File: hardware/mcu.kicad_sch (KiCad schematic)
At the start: 0 parts

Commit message: MBR0.0.1 - Begin addition of sheet pins to MCU page
Incomplete
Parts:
- added U1: STM32H503RBTx, Package_QFP:LQFP-64_10x10mm_P0.5mm, symbol MCU_ST_STM32H5:STM32H503RBTx
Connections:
- new net: U1.18 (VSS), U1.31 (VSS), U1.47 (VSS), U1.63 (VSS)
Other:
- note added: "Indicates if any thermal switches are open"
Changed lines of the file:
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@@
 	(generator "eeschema")
 	(generator_version "10.0")
-	(paper "A4")
+	(paper "B")
 	(title_block
 		(title "[BOARD NAME]")
@@
 		(company "Formula Slug")
 	)
-)

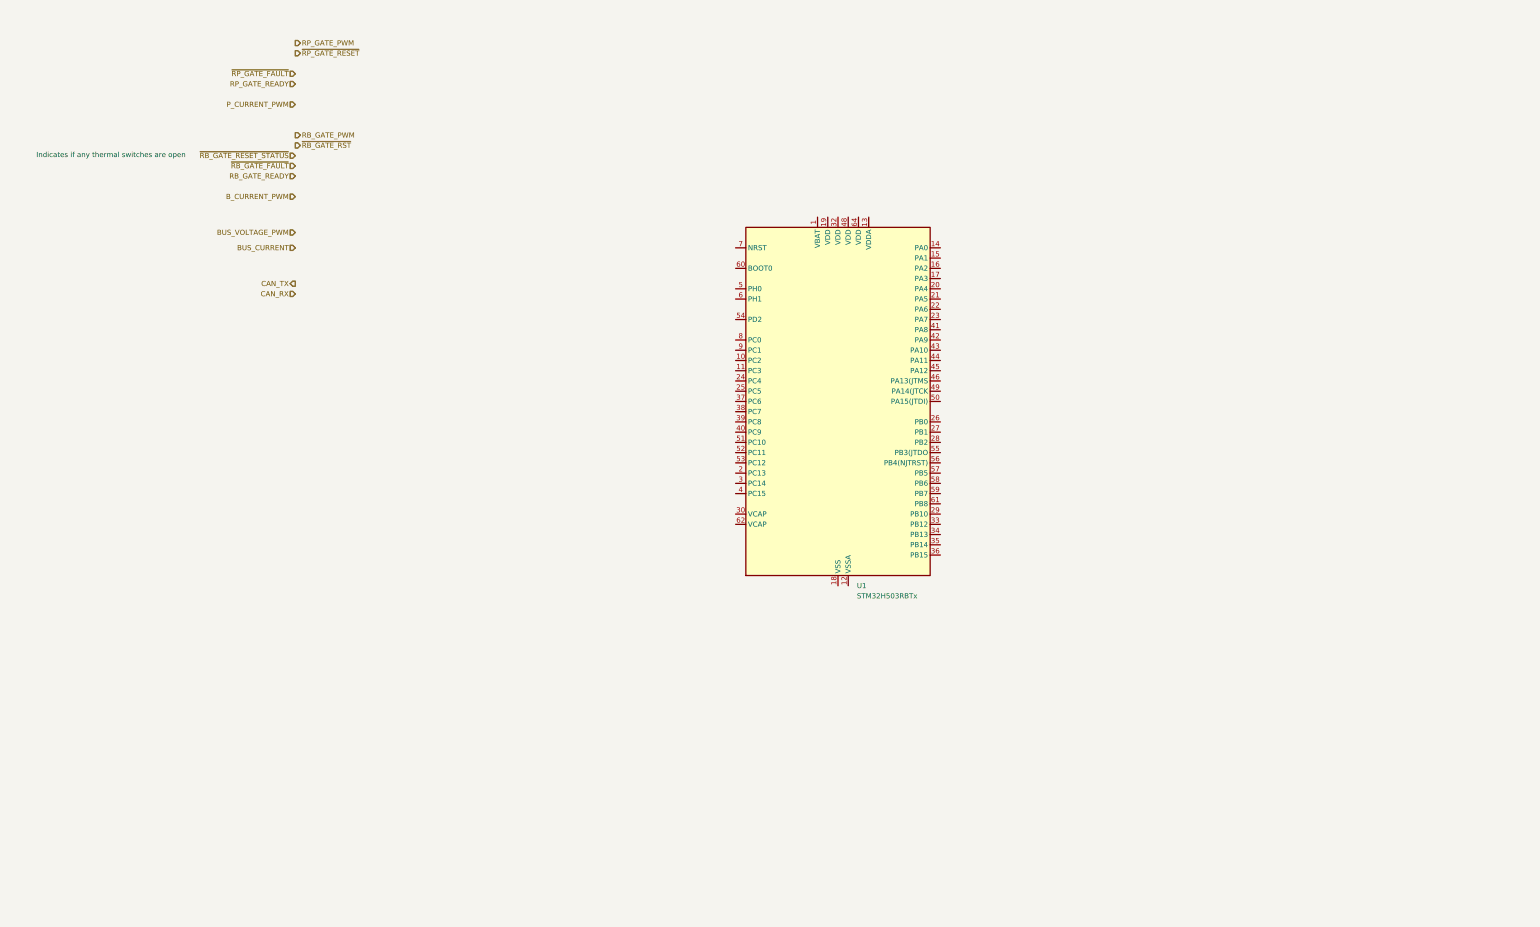
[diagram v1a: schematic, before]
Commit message: R0.0.2 Add more connections to MCU, some connectors
commit d1f92fde9a9b01f608e388bb27e003f4547c4ba5
Author: fezboy <31973884+fezboy@users.noreply.github.com>
Date:   Tue Apr 28 12:29:51 2026 -0700

    R0.0.2 Add more connections to MCU, some connectors
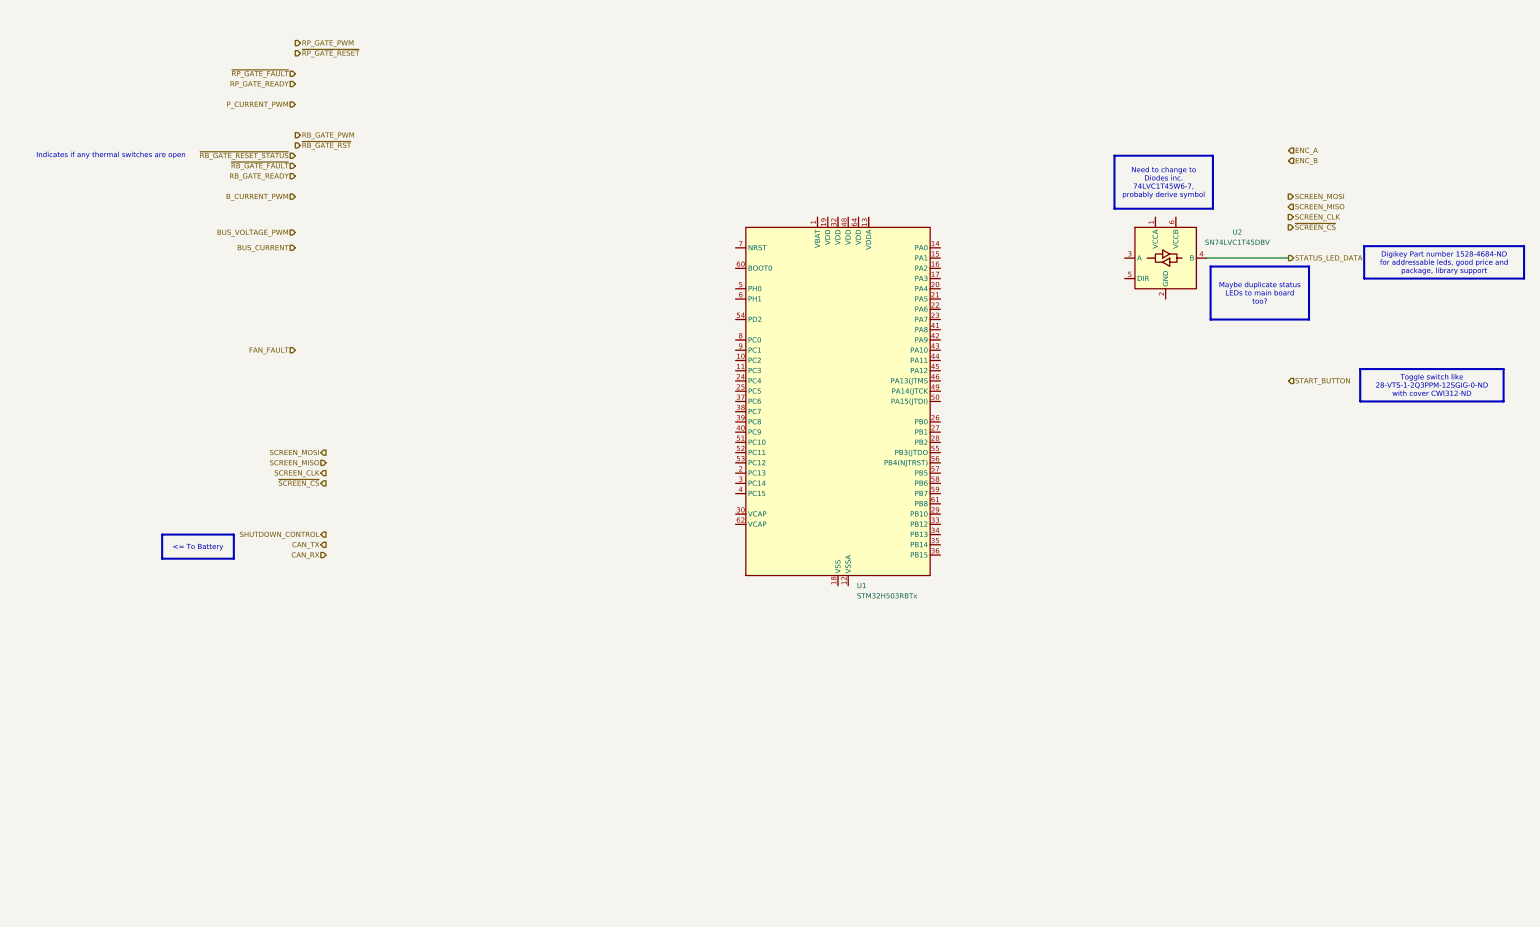
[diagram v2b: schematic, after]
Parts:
- added U2: SN74LVC1T45DBV, Package_TO_SOT_SMD:SOT-23-6, symbol Logic_LevelTranslator:SN74LVC1T45DBV
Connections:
- new net STATUS_LED_DATA: U2.4 (B)
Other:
- title: [BOARD NAME] -> Discharger Main Board
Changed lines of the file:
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@@
 	(paper "B")
 	(title_block
-		(title "[BOARD NAME]")
-		(date "[DATE]")
-		(rev "[REVISION]")
+		(title "Discharger Main Board")
+		(date "2026-04-23")
+		(rev "0.0.2")
 		(company "Formula Slug")
 	)

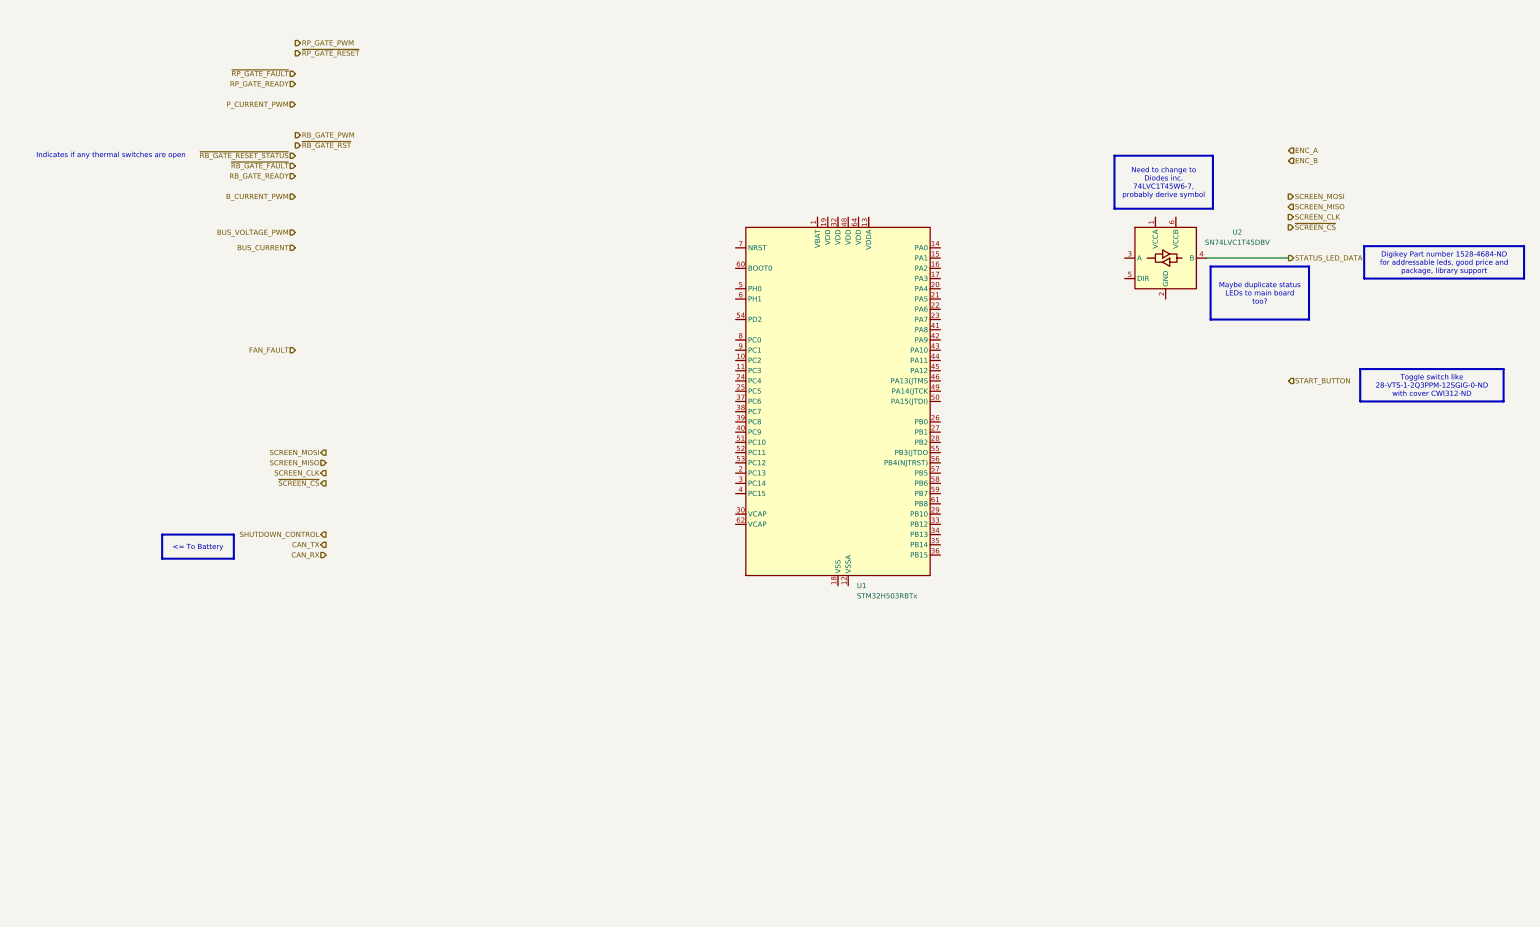
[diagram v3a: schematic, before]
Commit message: Start work on MCU Connections
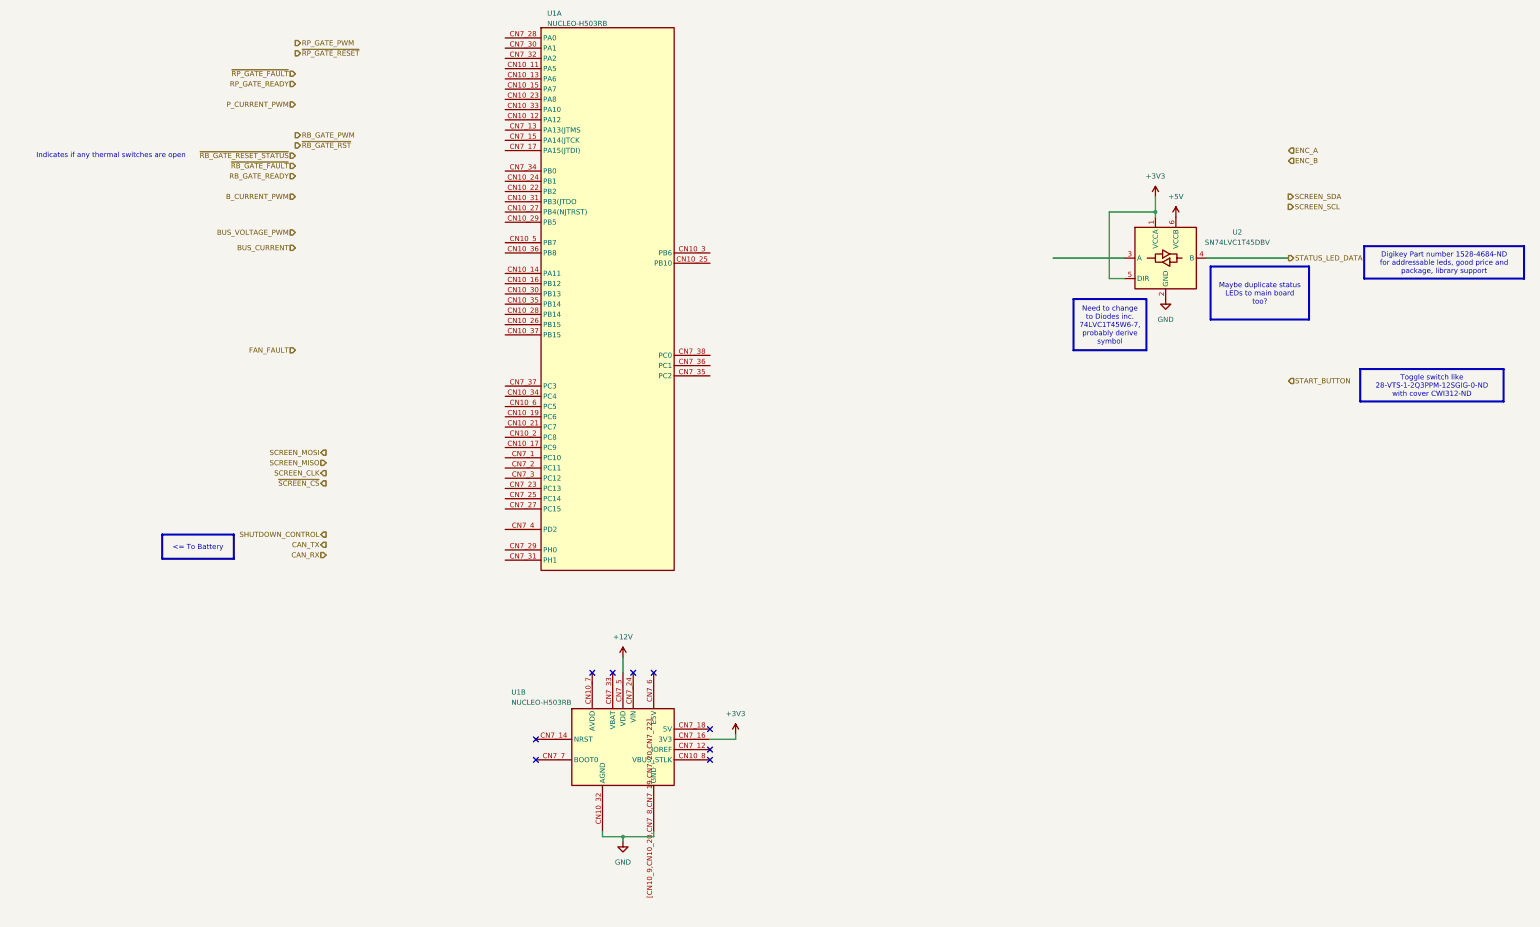
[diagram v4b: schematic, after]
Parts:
- removed U1: STM32H503RBTx, Package_QFP:LQFP-64_10x10mm_P0.5mm, symbol MCU_ST_STM32H5:STM32H503RBTx
- added U1: NUCLEO-H503RB, discharger:NUCLEO-H503RB, symbol discharger:NUCLEO-H503RB
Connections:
- net +3V3: now reaches U2.1 (VCCA)
- net +3V3: now also U2.5 (DIR), U1.CN7_16 (3V3)
- net GND: now reaches U2.2 (GND)
- net GND: now also U1.CN10_32 (AGND), U1.[CN10_9,CN10_20,CN7_8,CN7_19,CN7_20,CN7_22] (GND)
- net +5V: now reaches U2.6 (VCCB)
- new net: U1.CN10_1, U1.CN10_10, U1.CN10_18, U1.CN10_38, U1.CN10_4
- new net: U1.CN7_10, U1.CN7_11, U1.CN7_21, U1.CN7_26, U1.CN7_9
- new net +12V: U1.CN7_5 (VDD)
- no-connect marks 0 -> 9

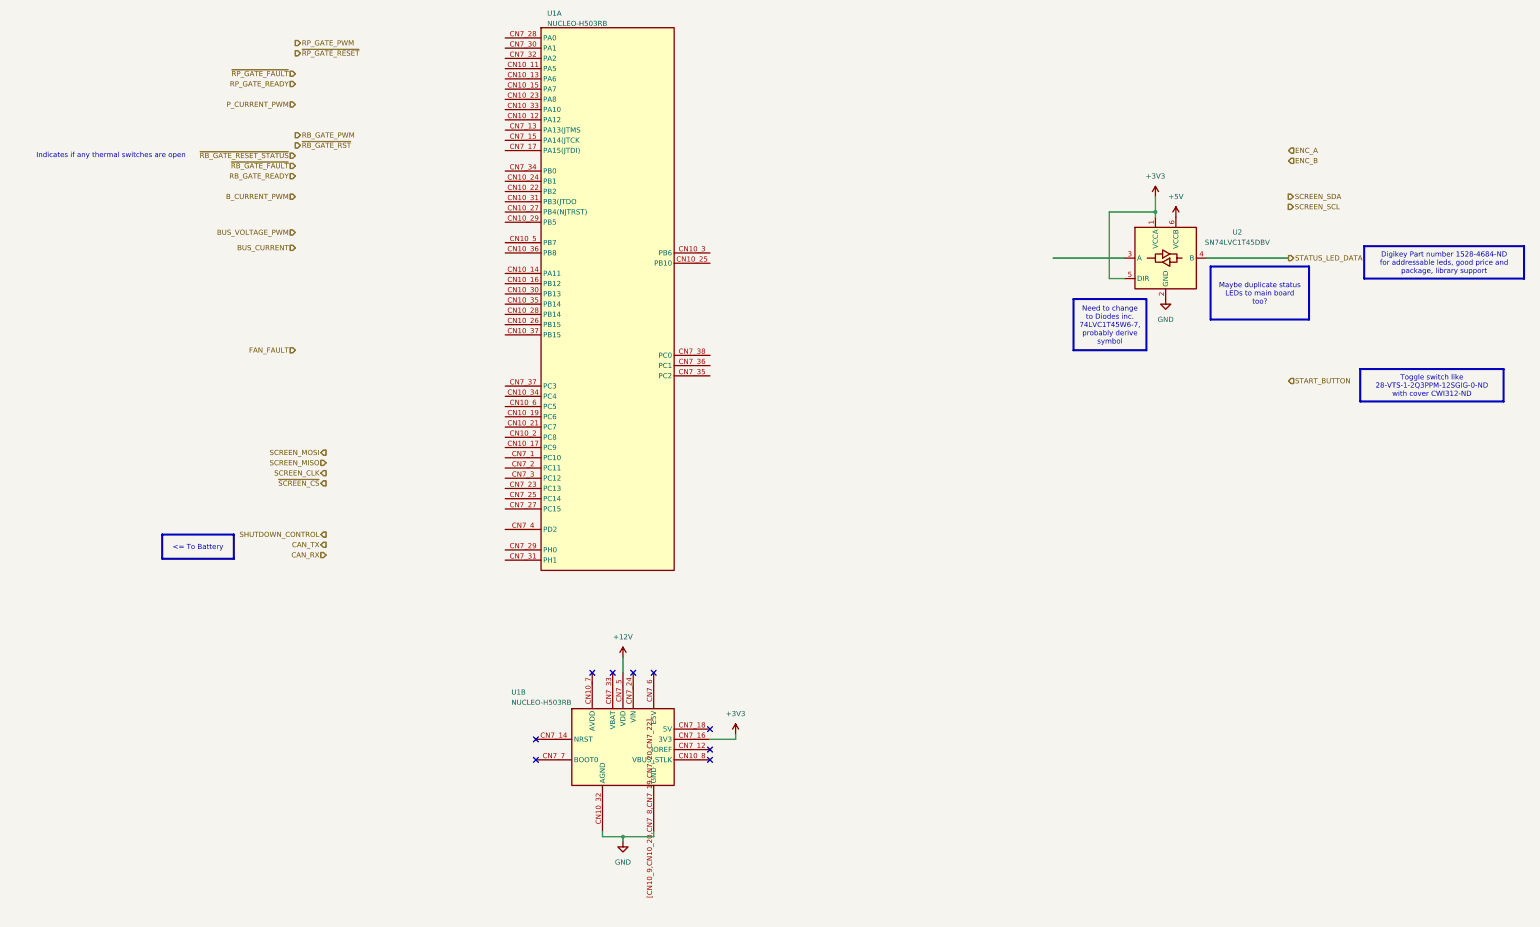
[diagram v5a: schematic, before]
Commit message: Pin assignment first draft
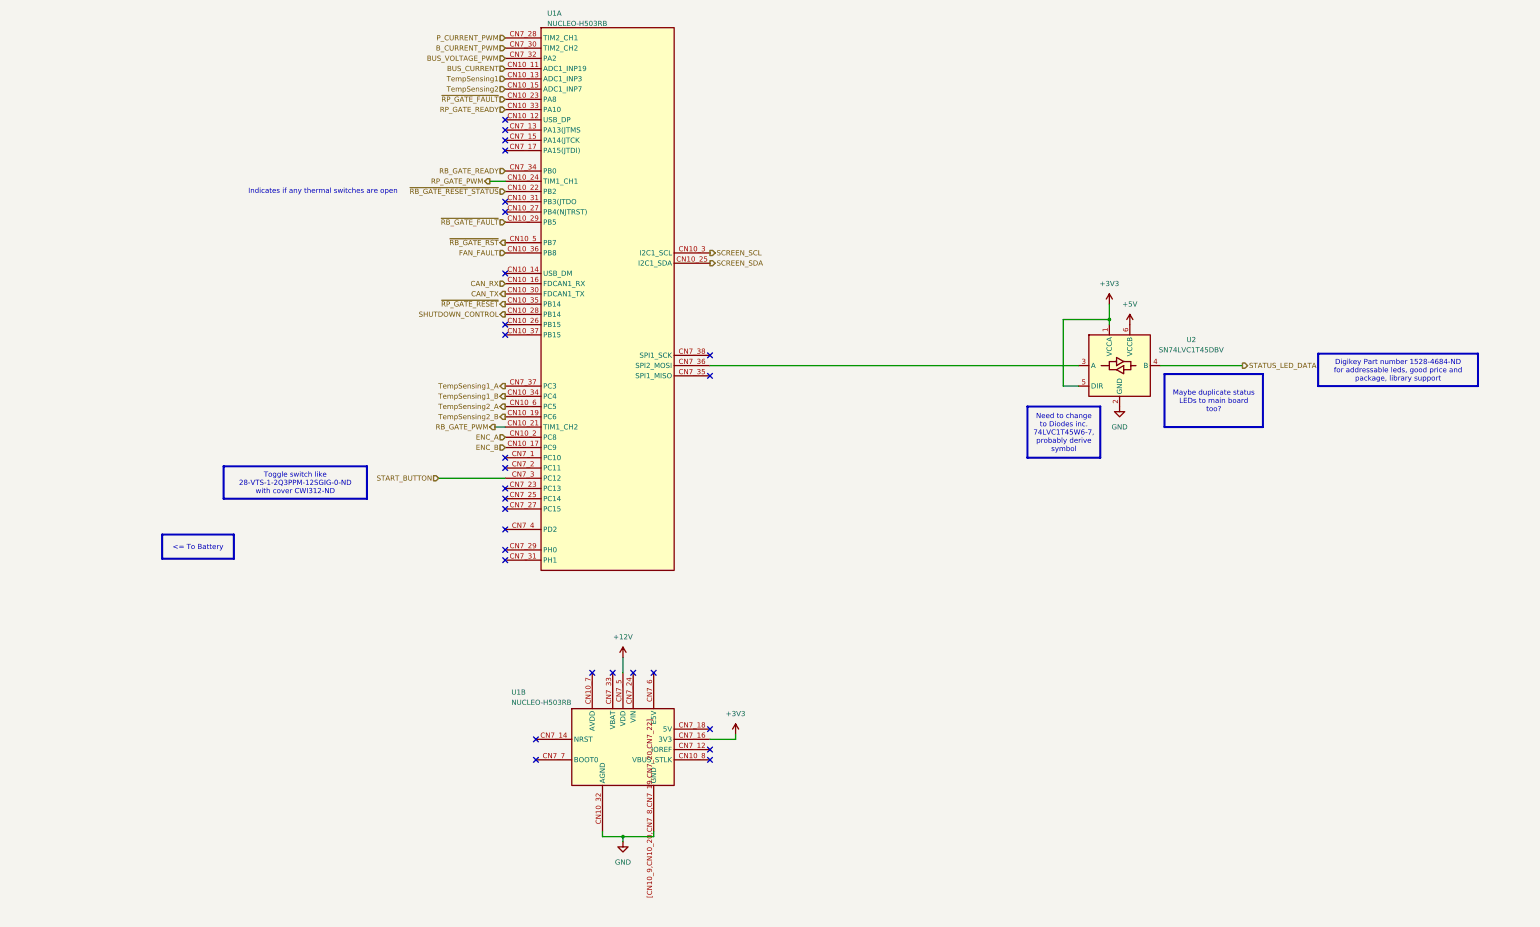
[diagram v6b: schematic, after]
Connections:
- net BUS_CURRENT: now also U1.CN10_11 (PA5)
- net BUS_VOLTAGE_PWM: now also U1.CN7_32 (PA2)
- net B_CURRENT_PWM: now also U1.CN7_30 (PA1)
- net CAN_RX: now also U1.CN10_16 (PB12)
- net CAN_TX: now also U1.CN10_30 (PB13)
- net ENC_A: now also U1.CN10_2 (PC8)
- net ENC_B: now also U1.CN10_17 (PC9)
- net FAN_FAULT: now also U1.CN10_36 (PB8)
- net P_CURRENT_PWM: now also U1.CN7_28 (PA0)
- net RB_GATE_PWM: now also U1.CN10_21 (PC7)
- net RB_GATE_READY: now also U1.CN7_34 (PB0)
- net RP_GATE_PWM: now also U1.CN10_24 (PB1)
- net RP_GATE_READY: now also U1.CN10_33 (PA10)
- net SCREEN_SCL: now also U1.CN10_3 (PB6)
- net SCREEN_SDA: now also U1.CN10_25 (PB10)
- net SHUTDOWN_CONTROL: now also U1.CN10_28 (PB14)
- net START_BUTTON: now also U1.CN7_3 (PC12)
- net ~{RB_GATE_FAULT}: now also U1.CN10_29 (PB5)
- net ~{RB_GATE_RESET_STATUS}: now also U1.CN10_22 (PB2)
- net ~{RB_GATE_RST}: now also U1.CN10_5 (PB7)
- net ~{RP_GATE_FAULT}: now also U1.CN10_23 (PA8)
- net ~{RP_GATE_RESET}: now also U1.CN10_35 (PB14)
- net at U2.3 (A): now also U1.CN7_36 (PC1)
- net TempSensing1: now reaches U1.CN10_13 (PA6)
- net TempSensing2: now reaches U1.CN10_15 (PA7)
- net TempSensing2_B: now reaches U1.CN10_19 (PC6)
- net TempSensing1_B: now reaches U1.CN10_34 (PC4)
- net TempSensing2_A: now reaches U1.CN10_6 (PC5)
- net TempSensing1_A: now reaches U1.CN7_37 (PC3)
- no-connect marks 9 -> 28
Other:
- moved on the sheet: U2
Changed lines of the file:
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@@
 	(title_block
 		(title "Discharger Main Board")
-		(date "2026-04-23")
-		(rev "0.0.3")
+		(date "2026-05-12")
+		(rev "0.0.4")
 		(company "Formula Slug")
 	)
